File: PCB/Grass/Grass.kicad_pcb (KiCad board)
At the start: 2 copper layers, 60 x 28 mm, 28 parts, among them U1 HT16K33-28SOP

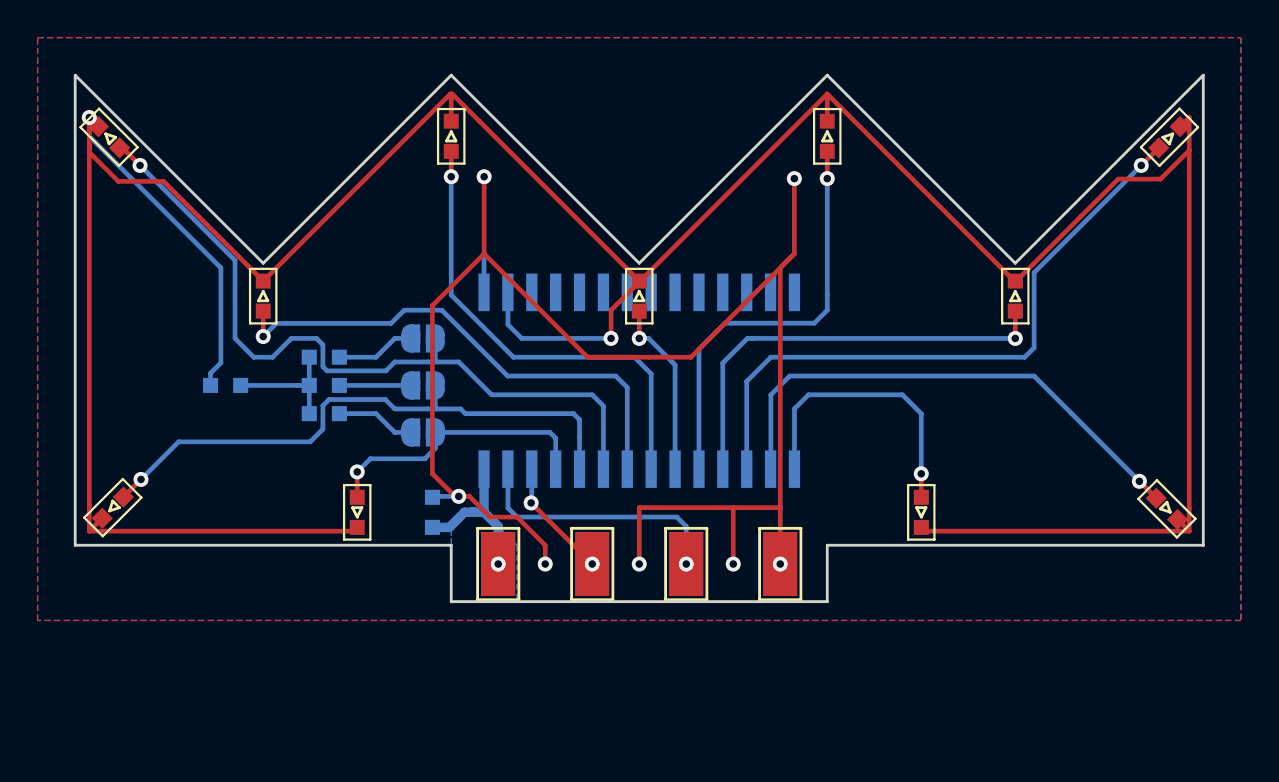
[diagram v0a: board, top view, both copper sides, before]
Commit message: [update] Grass v2.0登録
Grass v1.0->v2.0
コネクタ形状をカードエッジコネクタに対応
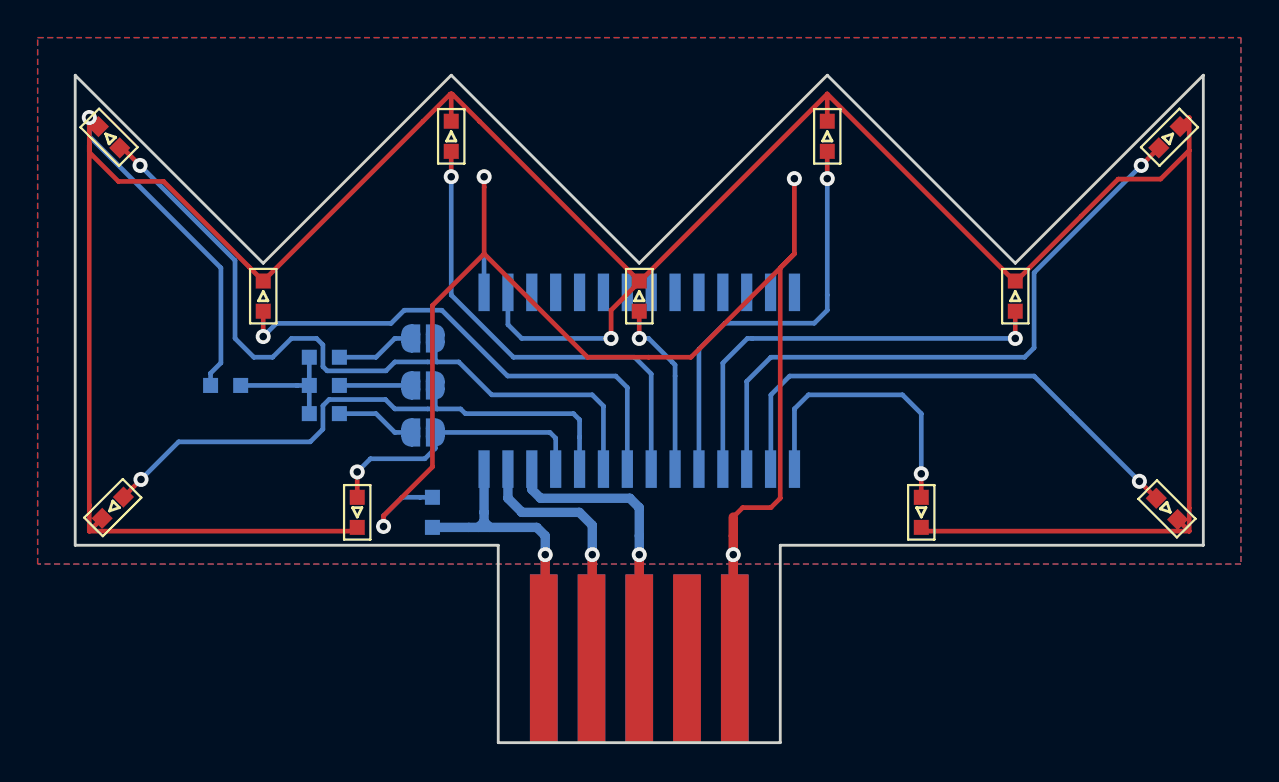
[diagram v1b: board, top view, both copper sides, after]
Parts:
- removed TP1, TP2, TP3, TP4, TP5, TP6, TP7, TP8: TestPoint, TestPoint:TestPoint_Keystone_5015_Micro-Minature
- added J1: Conn_01x05, extsui:EDAC_5P_P2.54mm, F.Cu at (130.0, 156.0)
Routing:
- net SCL: track 6.41 -> 20.7 mm, vias 2 -> 1
- net +5V: track 9.24 -> 21.9 mm
- net SDA: track 14.7 -> 19.9 mm
- net GND: track 84.3 -> 80.9 mm, vias 7 -> 4
- removed copper zone on B.Cu, net +5V
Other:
- board size 60 x 28 mm -> 60 x 35.5 mm
- board text added: "1"
- board text added: "5"
- board text added: "@ext_sui 2019.05"
- board text added: "Grass Growing v2.0"
- board text removed: "+5V"
- board text removed: "@ext_sui 2019.01"
- board text removed: "GND"
- board text removed: "Grass Growing v1.0"
- board text removed: "SCL"
- board text removed: "SDA"

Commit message: [update] Grass v2.1登録
Grass v2.0->v2.1
* カードエッジコネクタのPCBのパッドを'SMD'から'コネクタ'に修正
  (デフォルトライブラリのカードエッジコネクタ系を参考)
* コネクタ部の角を45度に修正
* コネクタ部のF.MaskとB.Maskの範囲を付け根までに修正
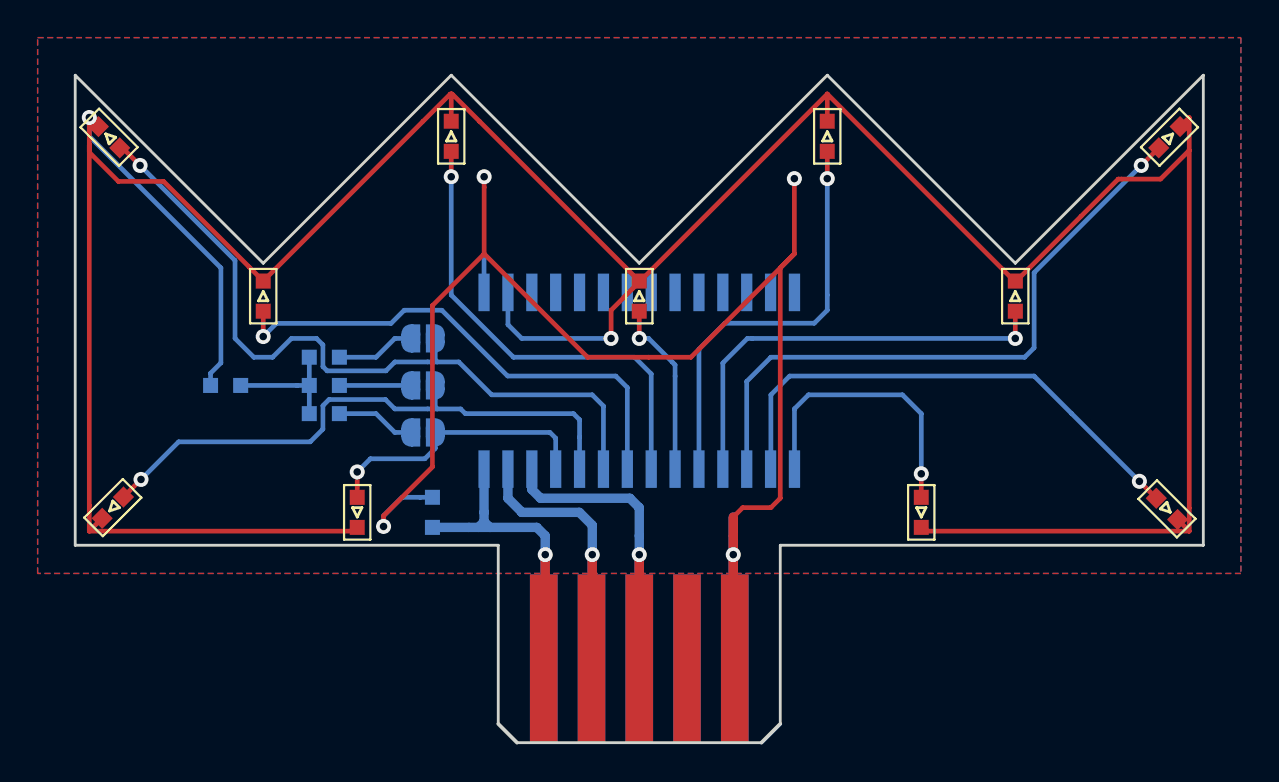
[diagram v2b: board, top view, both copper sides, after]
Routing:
- net GND: track 80.9 -> 82.9 mm
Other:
- outline, holes or cut-outs redrawn
- board text added: "@ext_sui 2019.11"
- board text added: "Grass Growing v2.1"
- board text removed: "@ext_sui 2019.05"
- board text removed: "Grass Growing v2.0"
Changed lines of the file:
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@@
   (general
     (thickness 1.6)
-    (drawings 21)
-    (tracks 246)
+    (drawings 23)
+    (tracks 247)
     (zones 0)
     (modules 21)
@@
   )
   (setup
-    (last_trace_width 0.5)
+    (last_trace_width 0.25)
     (user_trace_width 0.5)
     (user_trace_width 1)
@@
     (visible_elements 7FFFFFFF)
     (pcbplotparams
-      (layerselection 0x010f0_ffffffff)
+      (layerselection 0x010fc_ffffffff)
       (usegerberextensions true)
       (usegerberattributes false)
@@
     (add_net SDA)
   )
-  (module extsui:EDAC_5P_P2.54mm (layer F.Cu)
-    (at 130 156)
-    (fp_text reference J1 (at 0 -8.39) (layer F.SilkS) hide
-      (effects (font (size 1 1) (thickness 0.15)))
-    )
-    (fp_text value Conn_01x05 (at 0 -9.39) (layer F.Fab)
-      (effects (font (size 1 1) (thickness 0.15)))
-    )
-    (fp_line (start -7.47 4.445) (end 7.47 4.445) (layer F.CrtYd) (width 0.15))
-    (fp_line (start 7.47 4.445) (end 7.47 -6.045) (layer F.CrtYd) (width 0.15))
-    (fp_line (start -7.47 4.445) (end -7.47 -6.045) (layer F.CrtYd) (width 0.15))
-    (pad 1 smd rect (at -5.08 0) (size 1.47 8.89) (layers F.Cu F.Paste F.Mask)
-      (net 1 +5V))
-    (pad 2 smd rect (at -2.54 0) (size 1.47 8.89) (layers F.Cu F.Paste F.Mask)
-      (net 20 SDA))
-    (pad 3 smd rect (at 0 0) (size 1.47 8.89) (layers F.Cu F.Paste F.Mask)
-      (net 19 SCL))
-    (pad 4 smd rect (at 2.54 0) (size 1.47 8.89) (layers F.Cu F.Paste F.Mask)
-      (net 33 "Net-(J1-Pad4)"))
-    (pad 5 smd rect (at 5.08 0) (size 1.47 8.89) (layers F.Cu F.Paste F.Mask)
-      (net 2 GND))
-    (pad 1 smd rect (at -5.08 0) (size 1.47 8.89) (layers B.Cu B.Paste B.Mask)
-      (net 1 +5V))
-    (pad 2 smd rect (at -2.54 0) (size 1.47 8.89) (layers B.Cu B.Paste B.Mask)
-      (net 20 SDA))
-    (pad 3 smd rect (at 0 0) (size 1.47 8.89) (layers B.Cu B.Paste B.Mask)
-      (net 19 SCL))
-    (pad 4 smd rect (at 2.54 0) (size 1.47 8.89) (layers B.Cu B.Paste B.Mask)
-      (net 33 "Net-(J1-Pad4)"))
-    (pad 5 smd rect (at 5.08 0) (size 1.47 8.89) (layers B.Cu B.Paste B.Mask)
-      (net 2 GND))
-  )
   (module extsui:C_1608_HandSolderingCustom (layer B.Cu)
     (at 119 148.25 90)
@@
     )
   )
+  (module extsui:EDAC_5P_P2.54mm (layer F.Cu)
+    (at 130 156)
+    (fp_text reference J1 (at 0 -8.39) (layer F.SilkS) hide
+      (effects (font (size 1 1) (thickness 0.15)))
+    )
+    (fp_text value Conn_01x05 (at 0 -9.39) (layer F.Fab)
+      (effects (font (size 1 1) (thickness 0.15)))
+    )
+    (fp_line (start -7.47 4.445) (end 7.47 4.445) (layer F.CrtYd) (width 0.15))
+    (fp_line (start 7.47 4.445) (end 7.47 -6.045) (layer F.CrtYd) (width 0.15))
+    (fp_line (start -7.47 4.445) (end -7.47 -6.045) (layer F.CrtYd) (width 0.15))
+    (pad 1 connect rect (at -5.08 0) (size 1.47 8.89) (layers F.Cu F.Mask)
+      (net 1 +5V))
+    (pad 2 connect rect (at -2.54 0) (size 1.47 8.89) (layers F.Cu F.Mask)
+      (net 20 SDA))
+    (pad 3 connect rect (at 0 0) (size 1.47 8.89) (layers F.Cu F.Mask)
+      (net 19 SCL))
+    (pad 4 connect rect (at 2.54 0) (size 1.47 8.89) (layers F.Cu F.Mask)
+      (net 33 "Net-(J1-Pad4)"))
+    (pad 5 connect rect (at 5.08 0) (size 1.47 8.89) (layers F.Cu F.Mask)
+      (net 2 GND))
+    (pad 1 connect rect (at -5.08 0) (size 1.47 8.89) (layers B.Cu B.Mask)
+      (net 1 +5V))
+    (pad 2 connect rect (at -2.54 0) (size 1.47 8.89) (layers B.Cu B.Mask)
+      (net 20 SDA))
+    (pad 3 connect rect (at 0 0) (size 1.47 8.89) (layers B.Cu B.Mask)
+      (net 19 SCL))
+    (pad 4 connect rect (at 2.54 0) (size 1.47 8.89) (layers B.Cu B.Mask)
+      (net 33 "Net-(J1-Pad4)"))
+    (pad 5 connect rect (at 5.08 0) (size 1.47 8.89) (layers B.Cu B.Mask)
+      (net 2 GND))
+  )
+  (gr_line (start 136.5 160.5) (end 137.5 159.5) (layer Edge.Cuts) (width 0.2))
+  (gr_line (start 123.5 160.5) (end 122.5 159.5) (layer Edge.Cuts) (width 0.2))
   (dimension 35.5 (width 0.3) (layer F.CrtYd)
     (gr_text "35.500 mm" (at 91.9 142.75 90) (layer F.CrtYd)
@@
     (arrow2b (pts (xy 94 160.5) (xy 93.413579 159.373496)))
   )
-  (gr_poly (pts (xy 122.5 151.5) (xy 137.5 151.5) (xy 137.5 160.5) (xy 122.5 160.5)) (layer B.Mask) (width 0.15))
-  (gr_poly (pts (xy 122.5 151.5) (xy 137.5 151.5) (xy 137.5 160.5) (xy 122.5 160.5)) (layer F.Mask) (width 0.15))
+  (gr_poly (pts (xy 122.5 150) (xy 137.5 150) (xy 137.5 160.5) (xy 122.5 160.5)) (layer B.Mask) (width 0.15))
+  (gr_poly (pts (xy 122.5 150) (xy 137.5 150) (xy 137.5 160.5) (xy 122.5 160.5)) (layer F.Mask) (width 0.15))
   (gr_text 5 (at 135 149) (layer B.SilkS)
     (effects (font (size 1 1) (thickness 0.15)) (justify mirror))
@@
     (arrow2b (pts (xy 100.209094 163.843943) (xy 101.335598 163.257522)))
   )
-  (gr_text "@ext_sui 2019.05" (at 150 142.5) (layer B.SilkS)
+  (gr_text "@ext_sui 2019.11" (at 150 142.5) (layer B.SilkS)
     (effects (font (size 1 1) (thickness 0.2) italic) (justify mirror))
   )
-  (gr_text "Grass Growing v2.0" (at 150.5 140) (layer B.SilkS)
+  (gr_text "Grass Growing v2.1" (at 150.5 140) (layer B.SilkS)
     (effects (font (size 1 1) (thickness 0.25) italic) (justify mirror))
   )
-  (gr_line (start 122.5 150) (end 122.5 160.5) (layer Edge.Cuts) (width 0.15))
-  (gr_line (start 137.5 150) (end 137.5 160.5) (layer Edge.Cuts) (width 0.15))
-  (gr_line (start 122.5 160.5) (end 137.5 160.5) (layer Edge.Cuts) (width 0.15))
+  (gr_line (start 122.5 150) (end 122.5 159.5) (layer Edge.Cuts) (width 0.15))
+  (gr_line (start 137.5 150) (end 137.5 159.5) (layer Edge.Cuts) (width 0.15))
+  (gr_line (start 123.5 160.5) (end 136.5 160.5) (layer Edge.Cuts) (width 0.15))
   (gr_line (start 122.5 150) (end 100 150) (layer Edge.Cuts) (width 0.15))
   (gr_line (start 160 150) (end 137.5 150) (layer Edge.Cuts) (width 0.15))
@@
   (gr_line (start 100 125) (end 110 135) (layer Edge.Cuts) (width 0.15))
   (gr_line (start 100 150) (end 100 125) (layer Edge.Cuts) (width 0.15))
-  (via (at 116.4 149) (size 0.8) (drill 0.4) (layers F.Cu B.Cu) (net 2))
   (segment (start 121.745 145.95) (end 121.745 148.245) (width 0.5) (layer B.Cu) (net 1))
   (segment (start 119 149.05) (end 120.94 149.05) (width 0.5) (layer B.Cu) (net 1))
@@
   (segment (start 122.05 149.05) (end 124.55 149.05) (width 0.5) (layer B.Cu) (net 1))
   (segment (start 125 150.5) (end 125 149.5) (width 0.5) (layer B.Cu) (net 1))
+  (via (at 116.4 149) (size 0.8) (drill 0.4) (layers F.Cu B.Cu) (net 2))
   (segment (start 127.25 140) (end 130.5 140) (width 0.25) (layer F.Cu) (net 2))
   (segment (start 121.75 134.5) (end 127.25 140) (width 0.25) (layer F.Cu) (net 2))
@@
   (segment (start 119 137.25) (end 119 145.834315) (width 0.25) (layer F.Cu) (net 2))
   (segment (start 121.75 134.5) (end 119 137.25) (width 0.25) (layer F.Cu) (net 2))
+  (segment (start 135 150.5) (end 135 148.5) (width 0.5) (layer B.Cu) (net 2))
   (segment (start 121.5 127.45) (end 130 135.95) (width 0.25) (layer F.Cu) (net 3))
   (segment (start 157.724999 130.525001) (end 155.674999 130.525001) (width 0.25) (layer F.Cu) (net 3))
@@
     (polygon
       (pts
-        (xy 98 123) (xy 162 123) (xy 162 151) (xy 98 151)
+        (xy 98 123) (xy 162 123) (xy 162 151.5) (xy 98 151.5)
       )
     )
@@
     (polygon
       (pts
-        (xy 98 123) (xy 162 123) (xy 162 151) (xy 98 151)
+        (xy 98 123) (xy 162 123) (xy 162 151.5) (xy 98 151.5)
       )
     )
+  )
+  (zone (net 0) (net_name "") (layers F&B.Cu) (hatch edge 0.508)
+    (connect_pads (clearance 0.508))
+    (min_thickness 0.254)
+    (keepout (tracks allowed) (vias not_allowed) (copperpour not_allowed))
+    (fill (arc_segments 16) (thermal_gap 0.508) (thermal_bridge_width 0.508))
+    (polygon
+      (pts
+        (xy 120 149.4) (xy 140 149.4) (xy 140 151.4) (xy 120 151.4)
+      )
+    )
